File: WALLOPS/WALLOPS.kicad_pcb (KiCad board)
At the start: 2 copper layers, 55 x 67 mm, 25 parts, among them J1 JST-PH 1x9 Connector - WALLOP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, Q1 AO3401A, U1 VL53L8CX 0 (Zwicky), U2 VL58L8CX 1 (Aristotle), U3 VL53L8CX 3 (Copernicus), U4 VL53L8CX 2 (Brahe), U5 6DOF IMU (Sisko), U6 5V to 3.3V Converter

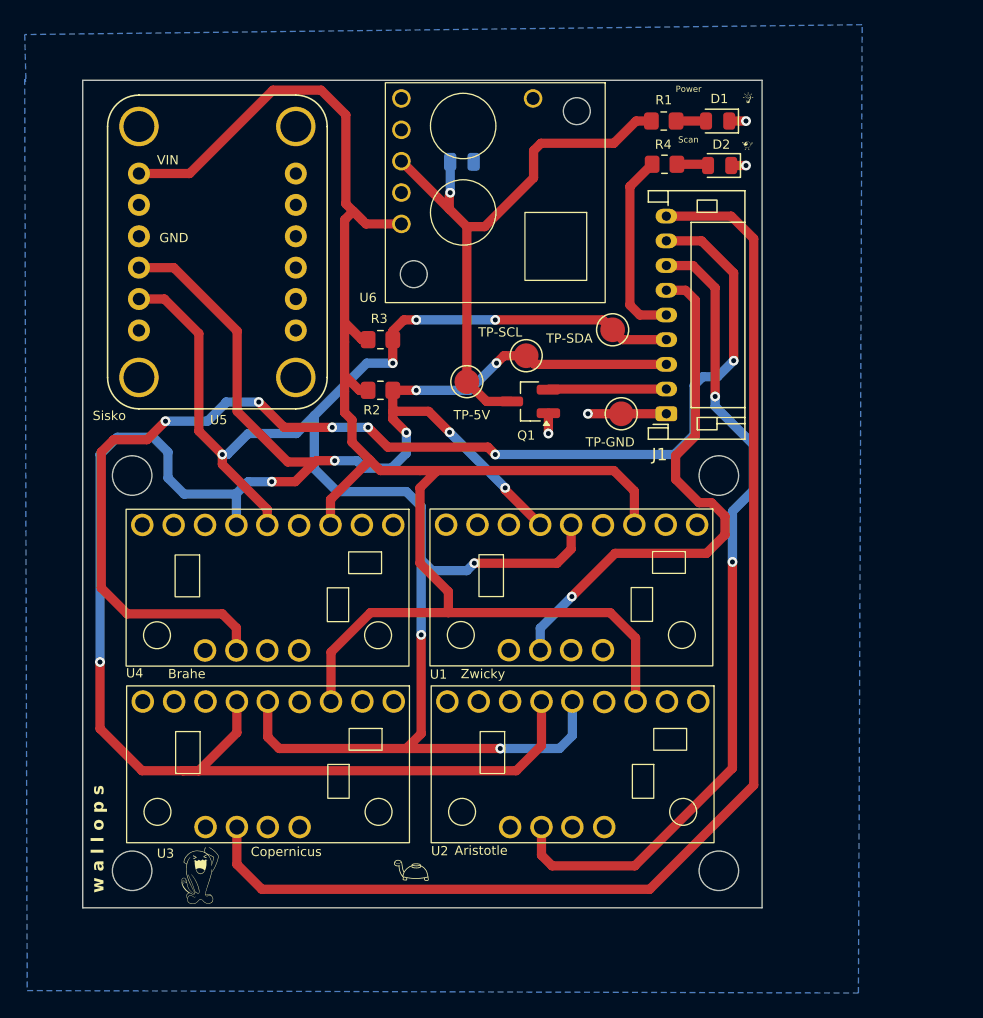
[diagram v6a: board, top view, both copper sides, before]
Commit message: Added individual TOF LPn pins to WALLOPS PCB
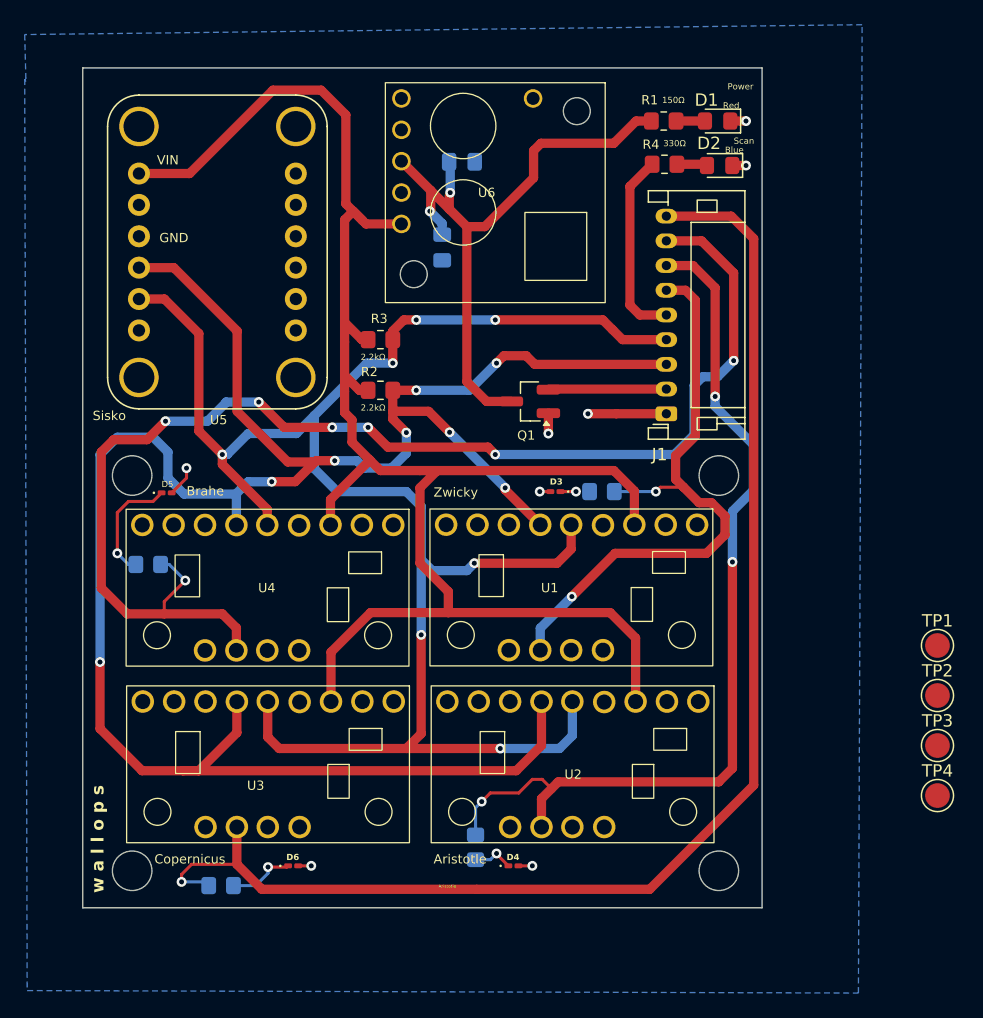
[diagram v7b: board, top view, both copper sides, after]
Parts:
- removed G*** (x6): LOGO, LOGO
- removed TP-5V: 5Vin_Test, RockSat:TestPoint_Pad_D2.0mm_With_Tolerance
- removed TP-GND: GND_TP, RockSat:TestPoint_Pad_D2.0mm_With_Tolerance
- removed TP-SCL: SCL_Test, RockSat:TestPoint_Pad_D2.0mm_With_Tolerance
- removed TP-SDA: SDA_Test, RockSat:TestPoint_Pad_D2.0mm_With_Tolerance
- added C2: 100nF, Capacitor_SMD:C_0805_2012Metric_Pad1.18x1.45mm_HandSolder, B.Cu at (189.1, 51.5)
- added D3: LPN0_PURPLE_LED, LED_SMD:LED_0201_0603Metric_Pad0.64x0.40mm_HandSolder, F.Cu at (198.3, 71.3)
- added D4: LPN1_PURPLE_LED, LED_SMD:LED_0201_0603Metric_Pad0.64x0.40mm_HandSolder, F.Cu at (194.9, 101.6)
- added D5: LPN2_PURPLE_LED, LED_SMD:LED_0201_0603Metric_Pad0.64x0.40mm_HandSolder, F.Cu at (166.8, 71.4)
- added D6: LPN3_PURPLE_LED, LED_SMD:LED_0201_0603Metric_Pad0.64x0.40mm_HandSolder, F.Cu at (177.0, 101.6)
- added R5: 33Ω, Resistor_SMD:R_0805_2012Metric_Pad1.20x1.40mm_HandSolder, B.Cu at (202.0, 71.3)
- added R6: 33Ω, Resistor_SMD:R_0805_2012Metric_Pad1.20x1.40mm_HandSolder, B.Cu at (191.8, 100.1)
- added R7: 33Ω, Resistor_SMD:R_0805_2012Metric_Pad1.20x1.40mm_HandSolder, B.Cu at (165.3, 77.2)
- added R8: 33Ω, Resistor_SMD:R_0805_2012Metric_Pad1.20x1.40mm_HandSolder, B.Cu at (171.2, 103.2)
- added TP1: GND_TP, RockSat:TestPoint_Pad_D2.0mm_With_Tolerance, F.Cu at (229.2, 83.8)
- added TP2: 5Vin_Test, RockSat:TestPoint_Pad_D2.0mm_With_Tolerance, F.Cu at (229.2, 87.8)
- added TP3: SCL_Test, RockSat:TestPoint_Pad_D2.0mm_With_Tolerance, F.Cu at (229.2, 91.9)
- added TP4: SDA_Test, RockSat:TestPoint_Pad_D2.0mm_With_Tolerance, F.Cu at (229.2, 95.9)
- C1: value 33µF -> 22µF; footprint Capacitor_SMD:C_0805_2012Metric -> Capacitor_SMD:C_0805_2012Metric_Pad1.18x1.45mm_HandSolder
- D1, D2: footprint LED_SMD:LED_0805_2012Metric -> LED_SMD:LED_0805_2012Metric_Pad1.15x1.40mm_HandSolder
- U1: value VL53L8CX 0 (Zwicky) -> VL53L8CX 0 (0x20; Zwicky)
- U2: value VL58L8CX 1 (Aristotle) -> VL58L8CX 1 (0x2A; Aristotle)
- U3: value VL53L8CX 3 (Copernicus) -> VL53L8CX 3 (0x2C; Copernicus)
- U4: value VL53L8CX 2 (Brahe) -> VL53L8CX 2 (0x2B; Brahe)
- U5: value 6DOF IMU (Sisko) -> 6DOF IMU (0x69; Sisko)
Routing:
- net Net-(D5-K): track 0.00 -> 9.42 mm, vias 0 -> 1
- net /LPn_3: track 101.3 -> 109.3 mm, vias 0 -> 1
- net /LPn_1: track 67.0 -> 74.0 mm, vias 2 -> 3
- net /LPn_2: track 98.9 -> 104.8 mm, vias 6 -> 7
- net /LPn_0: track 44.5 -> 50.2 mm, vias 1 -> 2
- net GND: track 10.6 -> 16.1 mm, vias 4 -> 8
- net Net-(D6-K): track 0.00 -> 5.38 mm, vias 0 -> 1
- net /5Vin: track 48.0 -> 52.0 mm, vias 1 -> 2
- net Net-(D4-K): track 0.00 -> 3.30 mm, vias 0 -> 1
- net Net-(D3-K): track 0.00 -> 2.36 mm, vias 0 -> 1
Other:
- board size 55 x 67 mm -> 55 x 68 mm
- board text added: "100nF"
- board text added: "150Ω"
- board text added: "2.2kΩ"
- board text added: "22µF"
- board text added: "330Ω"
- board text added: "33Ω"
- board text added: "Blue"
- board text added: "Red"

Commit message: Fixed WALLOPS JST-PH footprint; switched 0603 LEDs back to 0805
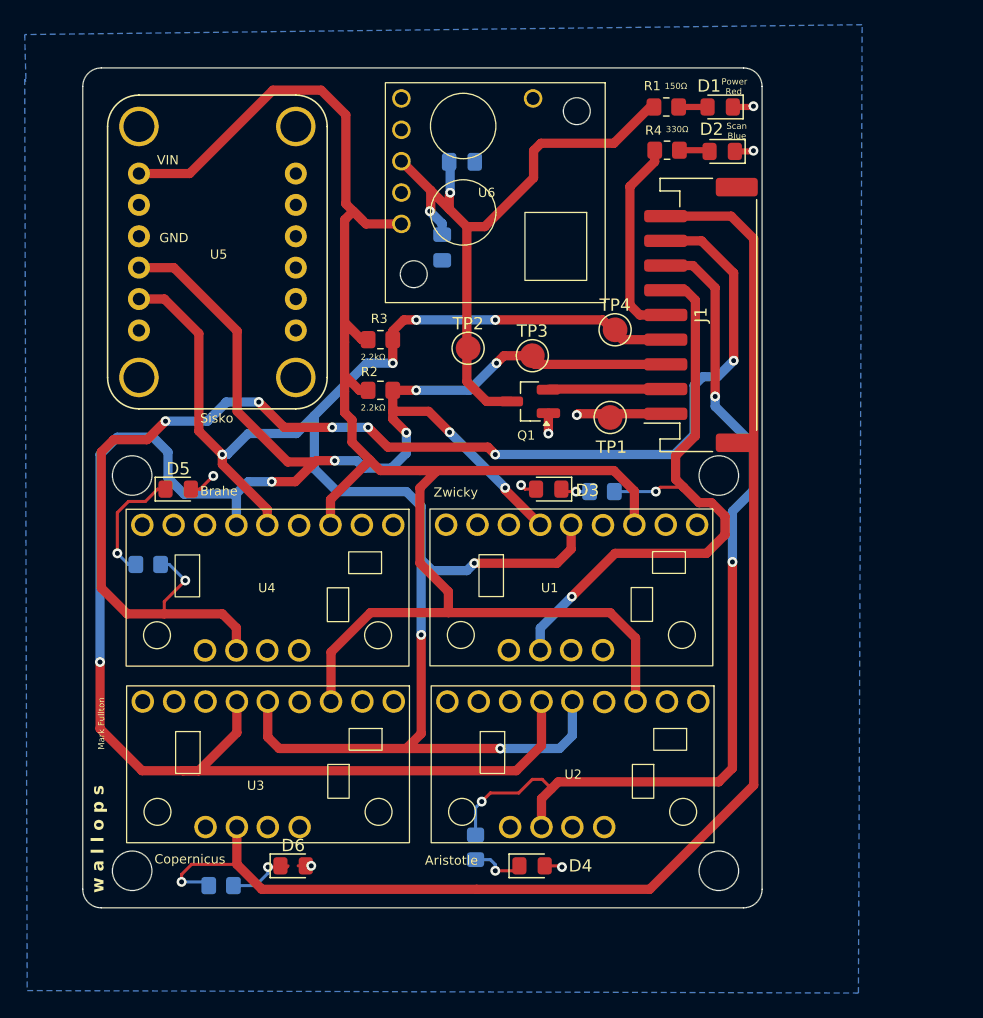
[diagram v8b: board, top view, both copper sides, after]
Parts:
- D3, D4, D5, D6: footprint LED_SMD:LED_0201_0603Metric_Pad0.64x0.40mm_HandSolder -> LED_SMD:LED_0805_2012Metric_Pad1.15x1.40mm_HandSolder
- J1: footprint Connector_JST:JST_PH_S9B-PH-K_1x09_P2.00mm_Horizontal -> Connector_JST:JST_PH_S9B-PH-SM4-TB_1x09-1MP_P2.00mm_Horizontal
- moved TP2 47.3 mm to (191.2, 59.7)
- moved TP4 45.9 mm to (203.1, 58.2)
- moved TP3 45.5 mm to (196.4, 60.3)
- moved TP1 32.3 mm to (202.7, 65.3)
- moved J1 8.48 mm to (210.1, 57.0)
- moved D4 1.51 mm to (196.4, 101.6)
- moved D2 1.16 mm to (211.8, 43.8)
- moved R1 1.16 mm to (207.2, 40.2)
- moved R4 1.16 mm to (207.3, 43.7)
- moved D1 1.16 mm to (211.6, 40.2)
- moved D5 0.98 mm to (167.7, 71.1)
- moved D3 0.58 mm to (197.7, 71.1)
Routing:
- net GND: track 16.1 -> 18.3 mm
- net /SCAN_LED: track 15.4 -> 16.7 mm
- net Net-(D4-K): track 3.30 -> 4.52 mm
- net /5Vin: track 52.0 -> 52.7 mm
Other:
- outline, holes or cut-outs redrawn
- board text added: "Mark Fullton"
